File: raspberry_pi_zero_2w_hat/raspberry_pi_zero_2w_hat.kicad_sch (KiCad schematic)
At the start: 6 parts, among them J1 GPIO, U1 CAT24C256

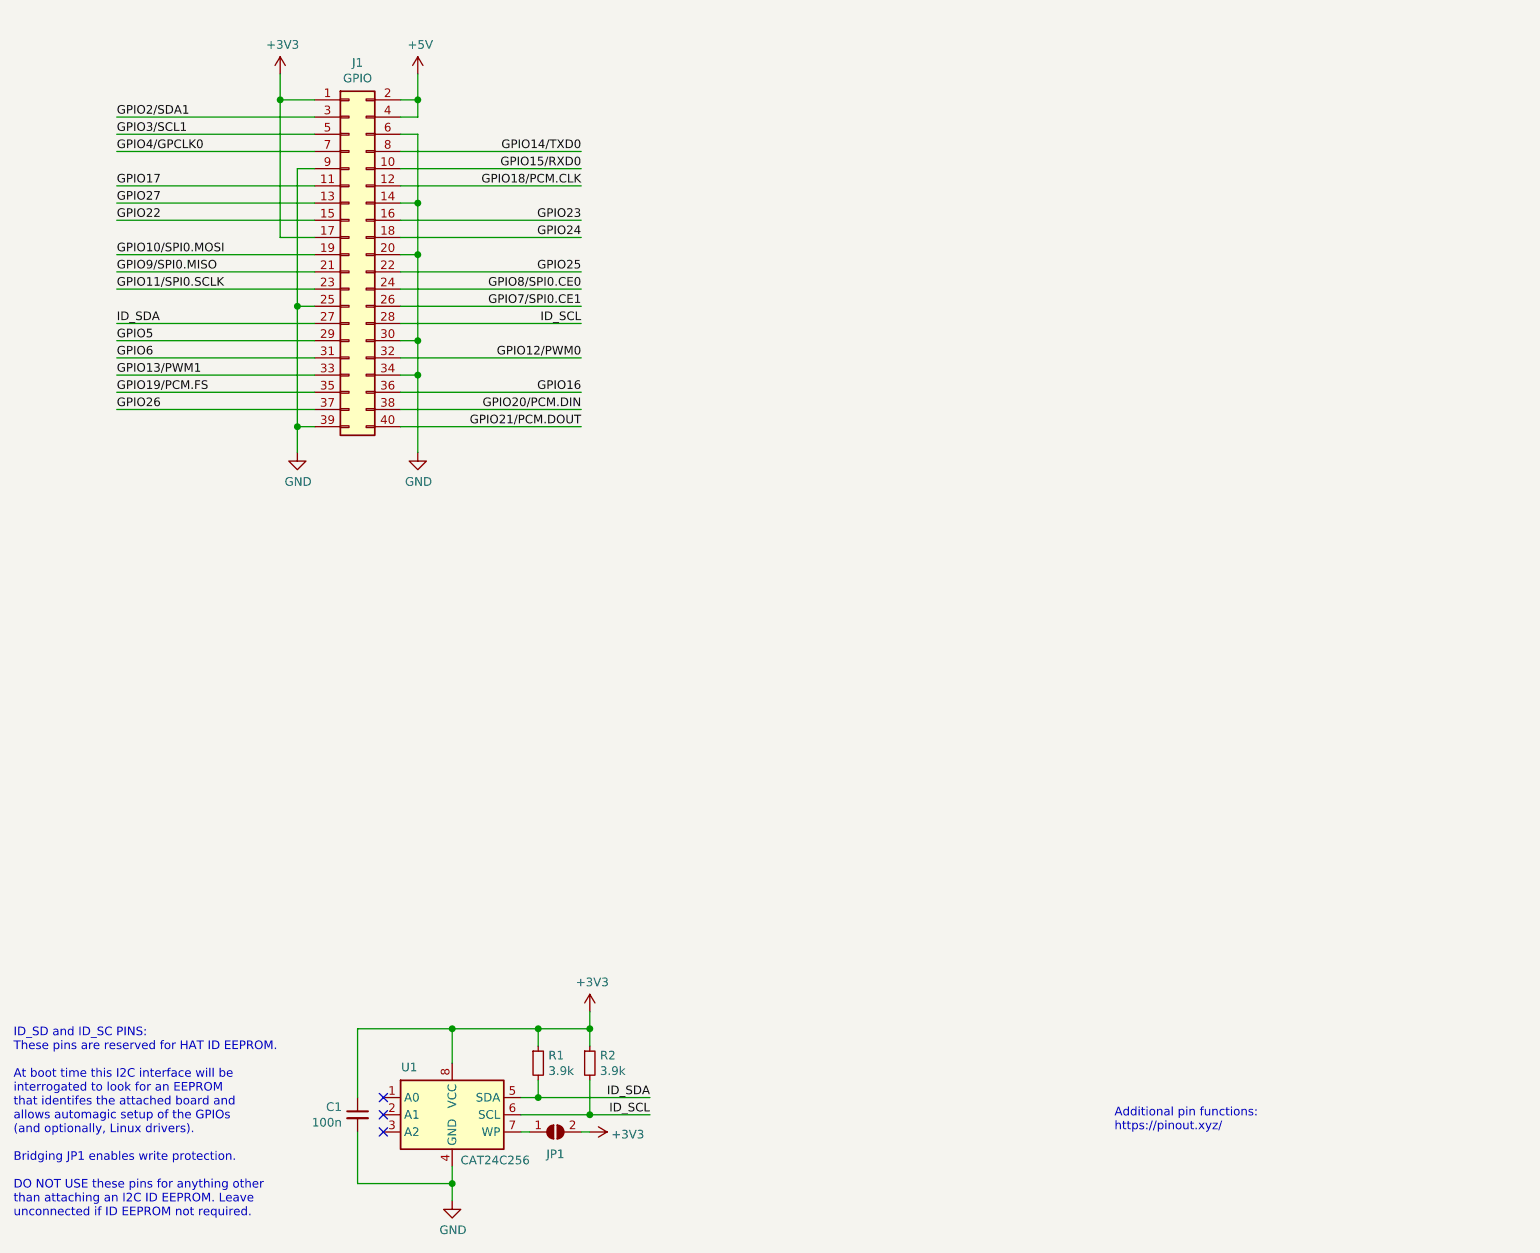
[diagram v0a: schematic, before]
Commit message: Added symbol and footprint libraries, connected rf module to hat in schematcs
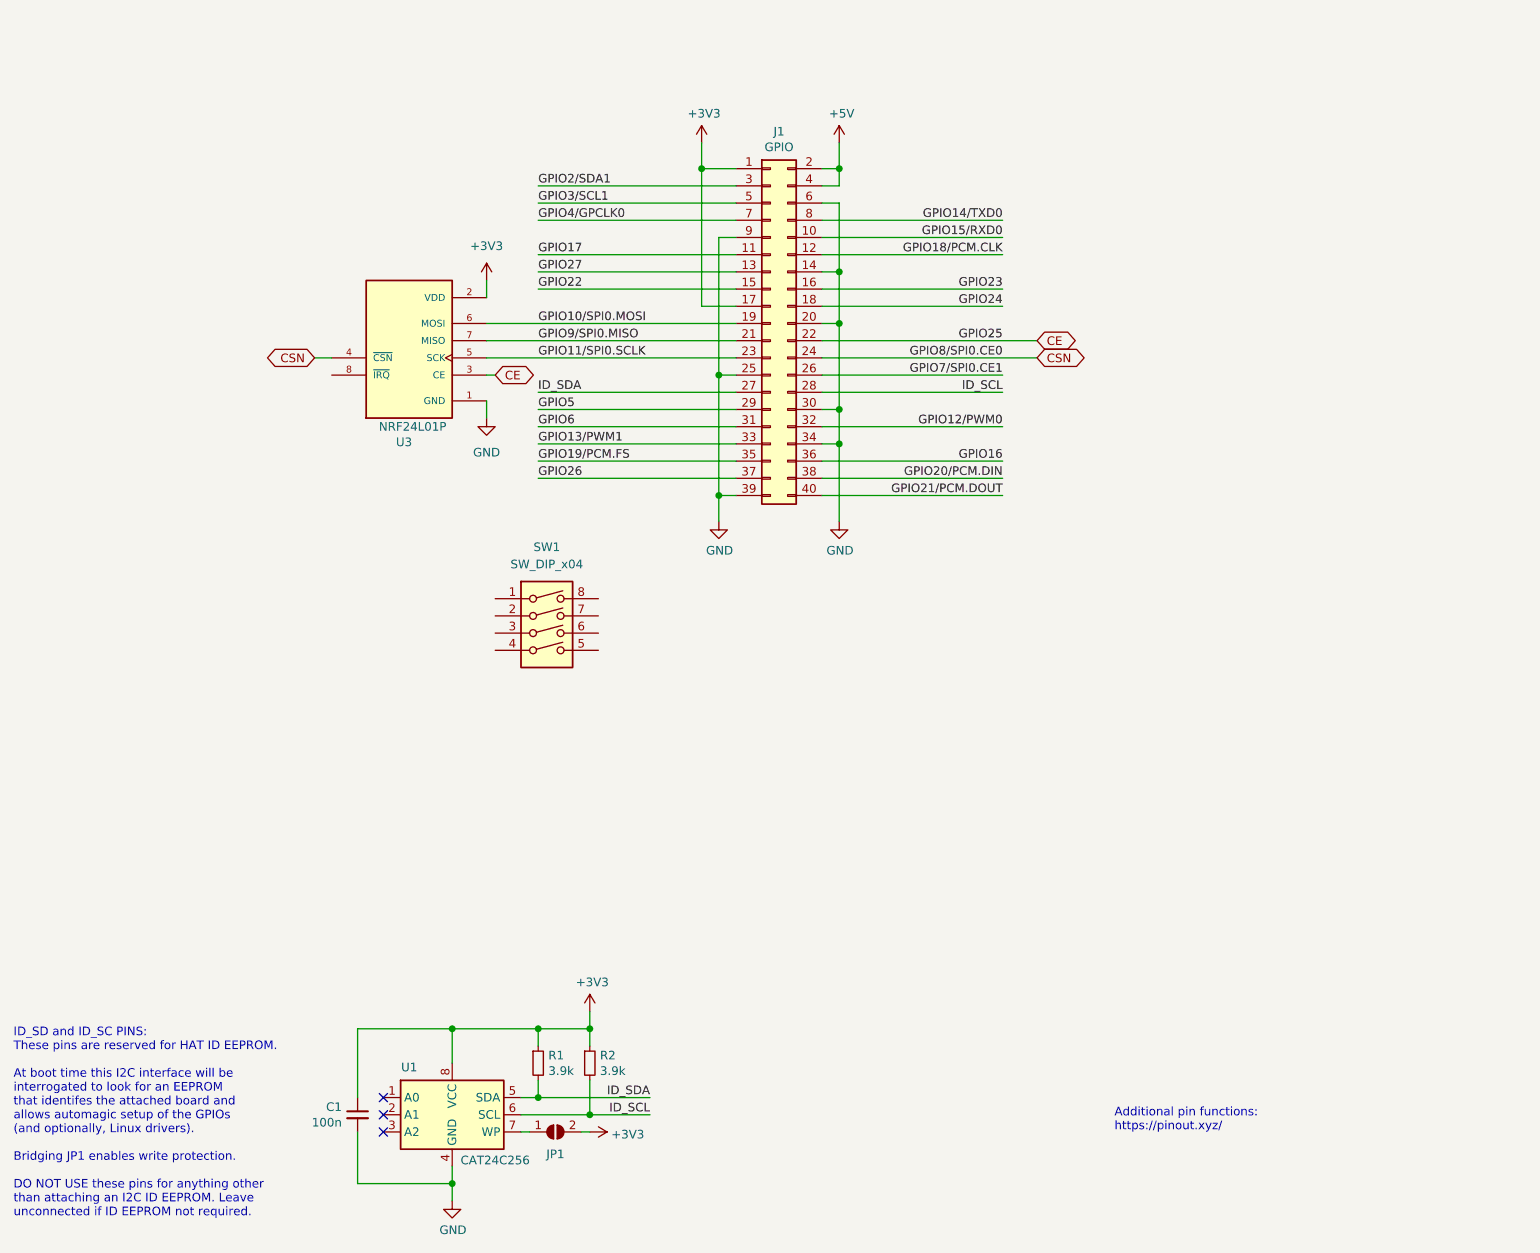
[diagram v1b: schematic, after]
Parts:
- added SW1: SW_DIP_x04, symbol Switch:SW_DIP_x04
- added U3: NRF24L01P, symbol NRF24L01P-MODULE-PCB:NRF24L01P-MODULE-PCB
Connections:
- net +3V3: now also U3.2 (VDD)
- net GND: now also U3.1 (GND)
- net GPIO10/SPI0.MOSI: now also U3.6 (MOSI)
- net GPIO11/SPI0.SCLK: now also U3.5 (SCK)
- net GPIO9/SPI0.MISO: now also U3.7 (MISO)
- net GPIO25 renamed CE
- net CE: now also U3.3 (CE)
- net GPIO8/SPI0.CE0 renamed CSN
- net CSN: now also U3.4 (~{CSN})
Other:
- moved on the sheet: J1

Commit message: Added decoupling capacitor for transceiver module
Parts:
- added C2: NRF_Decoup, Capacitor_THT:CP_Radial_D8.0mm_P5.00mm, symbol Device:C_Polarized_Small_US
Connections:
- net +3V3: now also C2.1
- net GND: now also C2.2
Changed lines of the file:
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@@
+	(wire
+		(pts
+			(xy 46.99 59.69) (xy 46.99 62.23)
+		)
+		(stroke
+			(width 0)
+			(type default)
+		)
+	)
 	(wire
 		(pts
@@
 			(width 0)
 			(type solid)
+		)
+	)
+	(wire
+		(pts
+			(xy 46.99 67.31) (xy 46.99 69.85)
+		)
+		(stroke
+			(width 0)
+			(type default)
 		)
 	)
@@
 	)
 	(symbol
+		(lib_name "GND_1")
+		(lib_id "power:GND")
+		(at 46.99 69.85 0)
+		(unit 1)
+		(exclude_from_sim no)
+		(in_bom yes)
+		(on_board yes)
+		(dnp no)
+		(fields_autoplaced yes)
+		(property "Reference" "#PWR08"
+			(at 46.99 76.2 0)
+			(effects
+				(font
+					(size 1.27 1.27)
+				)
+				(hide yes)
+			)
+		)
+		(property "Value" "GND"
+			(at 46.99 74.93 0)
+			(effects
+				(font
+					(size 1.27 1.27)
+				)
+			)
+		)
+		(property "Footprint" ""
+			(at 46.99 69.85 0)
+			(effects
+				(font
+					(size 1.27 1.27)
+				)
+				(hide yes)
+			)
+		)
+		(property "Datasheet" ""
+			(at 46.99 69.85 0)
+			(effects
+				(font
+					(size 1.27 1.27)
+				)
+				(hide yes)
+			)
+		)
+		(property "Description" "Power symbol creates a global label with name \"GND\" , ground"
+			(at 46.99 69.85 0)
+			(effects
+				(font
+					(size 1.27 1.27)
+				)
+				(hide yes)
+			)
+		)
+		(pin "1"
+		)
+		(instances
+			(project "raspberry_pi_zero_2w_hat"
+				(path "/e63e39d7-6ac0-4ffd-8aa3-1841a4541b55"
+					(reference "#PWR08")
+					(unit 1)
+				)
+			)
+		)
+	)
+	(symbol
 		(lib_id "Device:R_Small")
 		(at 93.98 170.18 0)
@@
 				(path "/e63e39d7-6ac0-4ffd-8aa3-1841a4541b55"
 					(reference "U1")
+					(unit 1)
+				)
+			)
+		)
+	)
+	(symbol
+		(lib_id "Device:C_Polarized_Small_US")
+		(at 46.99 64.77 0)
+		(mirror y)
+		(unit 1)
+		(exclude_from_sim no)
+		(in_bom yes)
+		(on_board yes)
+		(dnp no)
+		(property "Reference" "C2"
+			(at 44.45 63.0681 0)
+			(effects
+				(font
+					(size 1.27 1.27)
+				)
+				(justify left)
+			)
+		)
+		(property "Value" "NRF_Decoup"
+			(at 44.45 65.6081 0)
+			(effects
+				(font
+					(size 1.27 1.27)
+				)
+				(justify left)
+			)
+		)
+		(property "Footprint" "Capacitor_THT:CP_Radial_D8.0mm_P5.00mm"
+			(at 46.99 64.77 0)
+			(effects
+				(font
+					(size 1.27 1.27)
+				)
+				(hide yes)
+			)
+		)
+		(property "Datasheet" "~"
+			(at 46.99 64.77 0)
+			(effects
+				(font
+					(size 1.27 1.27)
+				)
+				(hide yes)
+			)
+		)
+		(property "Description" "Polarized capacitor, small US symbol"
+			(at 46.99 64.77 0)
+			(effects
+				(font
+					(size 1.27 1.27)
+				)
+				(hide yes)
+			)
+		)
+		(pin "2"
+		)
+		(pin "1"
+		)
+		(instances
+			(project ""
+				(path "/e63e39d7-6ac0-4ffd-8aa3-1841a4541b55"
+					(reference "C2")
 					(unit 1)
 				)
@@
 					(unit 1)
 				)
+			)
+		)
+	)
+	(symbol
+		(lib_id "power:+3V3")
+		(at 46.99 59.69 0)
+		(unit 1)
+		(exclude_from_sim no)
+		(in_bom yes)
+		(on_board yes)
+		(dnp no)
+		(fields_autoplaced yes)
+		(property "Reference" "#PWR07"
+			(at 46.99 63.5 0)
+			(effects
+				(font
+					(size 1.27 1.27)
+				)
+				(hide yes)
+			)
+		)
+		(property "Value" "+3V3"
+			(at 46.99 54.61 0)
+			(effects
+				(font
+					(size 1.27 1.27)
+				)
+			)
+		)
+		(property "Footprint" ""
+			(at 46.99 59.69 0)
+			(effects
+				(font
+					(size 1.27 1.27)
+				)
+				(hide yes)
+			)
+		)
+		(property "Datasheet" ""
+			(at 46.99 59.69 0)
+			(effects
+				(font
+					(size 1.27 1.27)
+				)
+				(hide yes)
+			)
+		)
+		(property "Description" "Power symbol creates a global label with name \"+3V3\""
+			(at 46.99 59.69 0)
+			(effects
+				(font
+					(size 1.27 1.27)
+				)
+				(hide yes)
+			)
+		)
+		(pin "1"
+		)
+		(instances
+			(project "raspberry_pi_zero_2w_hat"
+				(path "/e63e39d7-6ac0-4ffd-8aa3-1841a4541b55"
+					(reference "#PWR07")
+					(unit 1)
+				)

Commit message: Added On-Off switch
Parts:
- added SW2: SW_Nidec_CAS-120A1, Button_Switch_SMD:SW_SPST_Omron_B3FS-100xP, symbol Switch:SW_Nidec_CAS-120A1
- C2: value NRF_Decoup -> 47uF
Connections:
- net GND: now also SW2.1 (C), SW2.2 (B)
- net GPIO3/SCL1: now also SW2.3 (A)

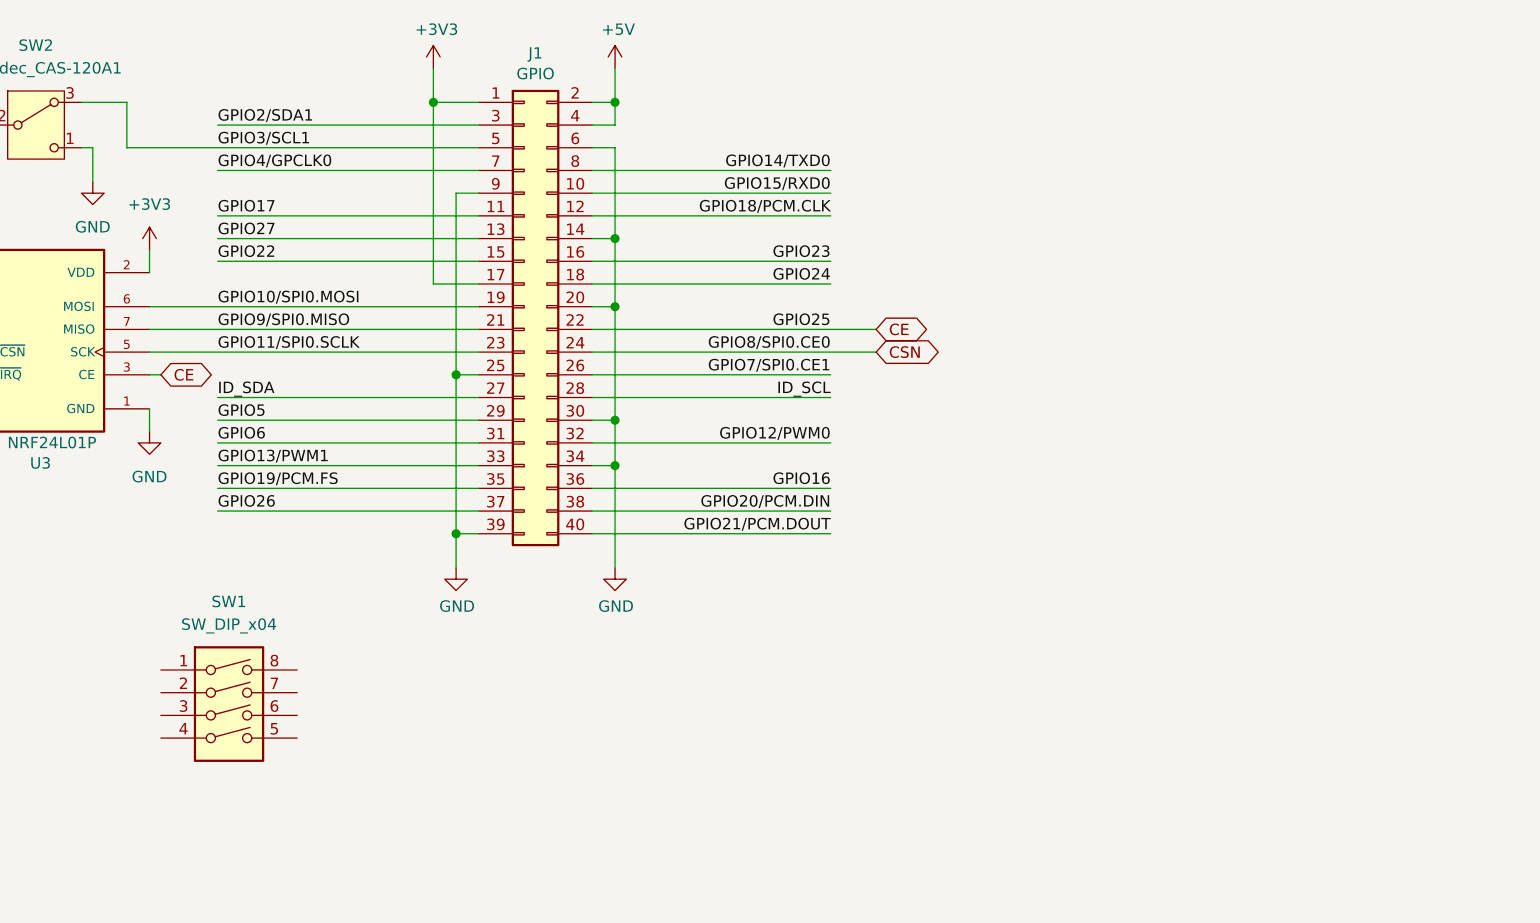
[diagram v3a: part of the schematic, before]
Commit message: Added status dipswuitch to schematics
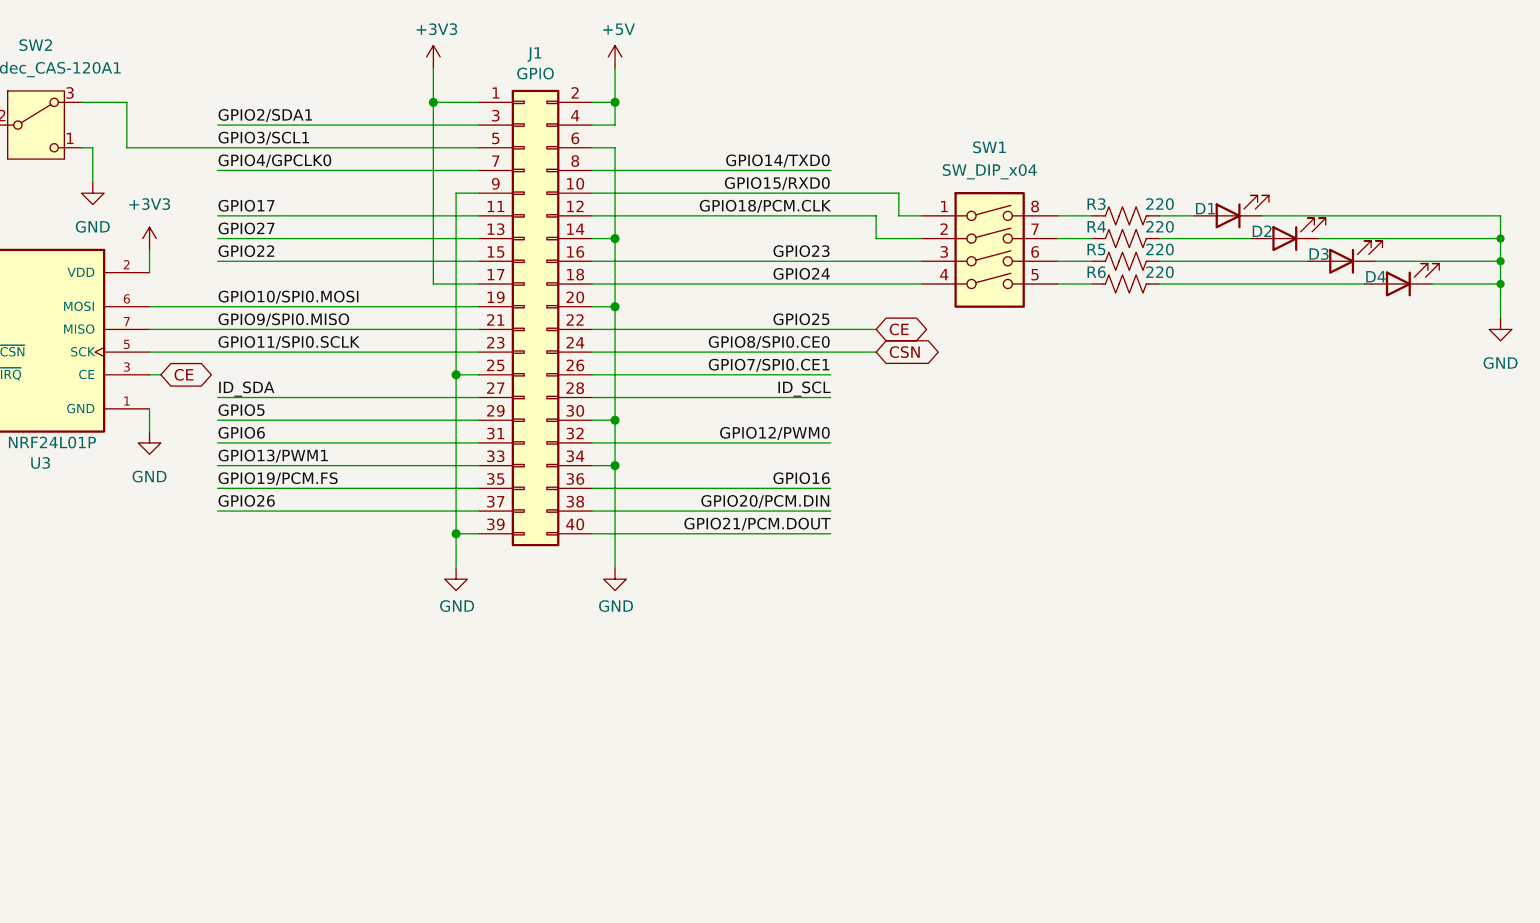
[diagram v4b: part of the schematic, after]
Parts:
- added D1: LED, LED_THT:LED_D5.0mm_Horizontal_O1.27mm_Z3.0mm, symbol Device:LED
- added D2, D3, D4: LED, symbol Device:LED
- added R3, R4, R5, R6: 220, Resistor_THT:R_Axial_DIN0516_L15.5mm_D5.0mm_P20.32mm_Horizontal, symbol Device:R_US
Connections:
- net GND: now also D1.1 (K), D2.1 (K), D3.1 (K), D4.1 (K)
- net GPIO15/RXD0: now also SW1.1
- net GPIO18/PCM.CLK: now also SW1.2
- net GPIO23: now also SW1.3
- net GPIO24: now also SW1.4
- net at SW1.5: now also R6.1
- net at SW1.6: now also R5.1
- net at SW1.7: now also R4.1
- net at SW1.8: now also R3.1
- new net: D4.2 (A), R6.2
- new net: D1.2 (A), R3.2
- new net: D3.2 (A), R5.2
- new net: D2.2 (A), R4.2
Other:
- moved on the sheet: SW1
